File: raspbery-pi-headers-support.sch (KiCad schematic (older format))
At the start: 15 parts, among them J1 RasPi-CM3-Headers, J10 500901-0801, J11 HDMI-A-connector, U38 DMG1012T, U39 DMG1012T, U40 ESD7484, U41 ESD7484, U42 ESD5384, U43 AP2331X

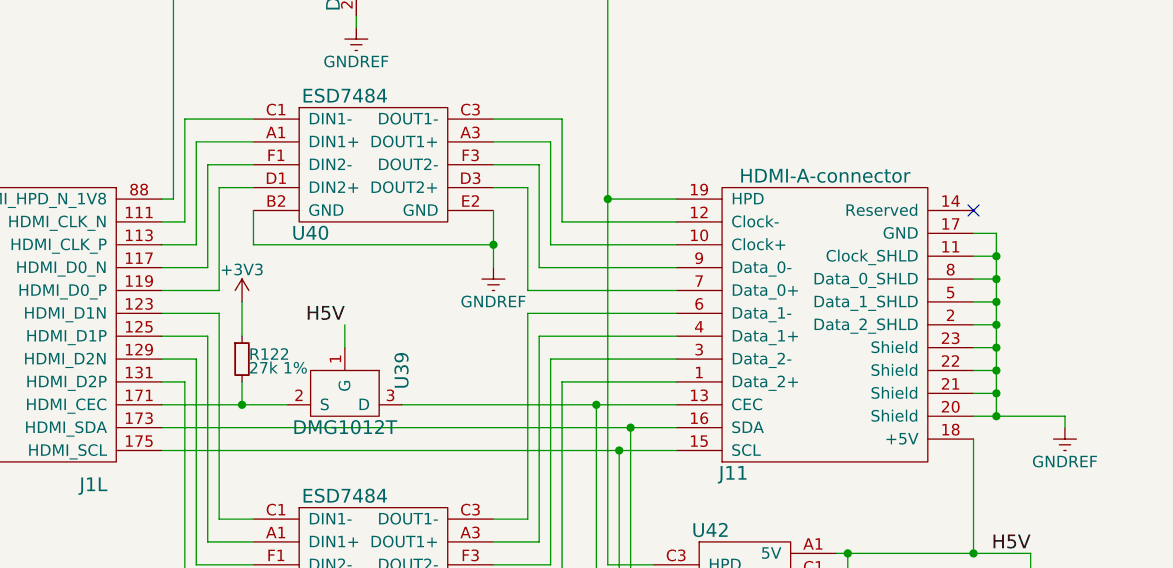
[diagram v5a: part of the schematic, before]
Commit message: Fixing issues with pin numbering between footprint and symbol
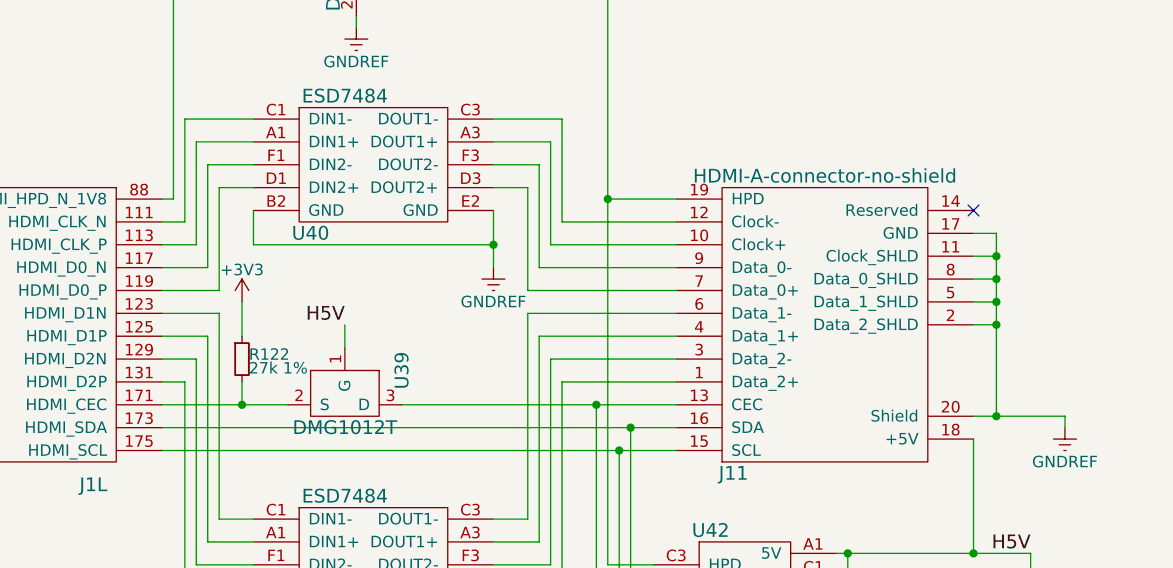
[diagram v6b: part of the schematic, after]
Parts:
- removed J11: HDMI-A-connector, Pin_Headers:Pin_Header_Straight_2x10_Pitch1.27mm, symbol HDMI-A-connector
- added J11: HDMI-A-connector-no-shield, Pin_Headers:Pin_Header_Straight_2x10_Pitch1.27mm, symbol HDMI-A-connector-no-shield
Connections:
- net GNDREF: now also J11.11 (Clock_SHLD), J11.17 (GND), J11.2 (Data_2_SHLD), J11.20 (Shield), J11.5 (Data_1_SHLD), J11.8 (Data_0_SHLD)
- net H5V: now also J11.18 (+5V)
- net at J1.173 (HDMI_SDA), U42.B3 (SDA): now also J11.16 (SDA)
- net at J1.175 (HDMI_SCL), U42.A3 (SCL): now also J11.15 (SCL)
- net at U41.D3 (DOUT2+): now also J11.1 (Data_2+)
- net at U40.A3 (DOUT1+): now also J11.10 (Clock+)
- net at U40.C3 (DOUT1-): now also J11.12 (Clock-)
- net at U39.3 (D), U42.A2 (CEC): now also J11.13 (CEC)
- net at U38.1 (G), U42.C3 (HPD): now also J11.19 (HPD)
- net at U41.F3 (DOUT2-): now also J11.3 (Data_2-)
- net at U41.A3 (DOUT1+): now also J11.4 (Data_1+)
- net at U41.C3 (DOUT1-): now also J11.6 (Data_1-)
- net at U40.D3 (DOUT2+): now also J11.7 (Data_0+)
- net at U40.F3 (DOUT2-): now also J11.9 (Data_0-)
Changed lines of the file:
@@
-$EndComp
-$Comp
-L HDMI-A-connector J11
-U 1 1 5911658C
-P 5450 2950
-F 0 "J11" H 5050 3600 60  0000 C CNN
-F 1 "HDMI-A-connector" H 5450 2300 60  0000 C CNN
-F 2 "Pin_Headers:Pin_Header_Straight_2x10_Pitch1.27mm" H 5450 2950 60  0001 C CNN
-F 3 "" H 5450 2950 60  0001 C CNN
-F 4 "0.00@0" H 5500 3850 60  0001 C CNN "Pricing"
-F 5 "Generic HDMI Connector pinout" H 5500 3750 60  0001 C CNN "Description"
-	1    5450 2950
-	1    0    0    1
 $EndComp
 $Comp
@@
 Wire Wire Line
 	6100 3350 6500 3350
-Wire Wire Line
-	6100 3250 6200 3250
-Connection ~ 6200 3250
-Wire Wire Line
-	6100 3150 6200 3150
-Connection ~ 6200 3150
-Wire Wire Line
-	6100 3050 6200 3050
-Connection ~ 6200 3050
 Wire Wire Line
 	6100 2950 6200 2950
@@
 $EndComp
 Wire Wire Line
-	3100 3300 2550 3300
+	2550 3300 3100 3300
 Text Label 3350 2950 2    60   ~ 0
 H5V
@@
 	2900 2850 2900 3000
 NoConn ~ 6100 2450
+$Comp
+L HDMI-A-connector-no-shield J11
+U 1 1 59200D14
+P 5450 2950
+F 0 "J11" H 5050 3600 60  0000 C CNN
+F 1 "HDMI-A-connector-no-shield" H 5450 2300 60  0000 C CNN
+F 2 "Pin_Headers:Pin_Header_Straight_2x10_Pitch1.27mm" H 5450 2950 60  0001 C CNN
+F 3 "" H 5450 2950 60  0001 C CNN
+F 4 "Generic HDMI Connector pinout" H 5500 3750 60  0001 C CNN "Description"
+F 5 "0.00@0" H 5500 3850 60  0001 C CNN "Pricing"
+	1    5450 2950
+	1    0    0    1
+$EndComp
 $EndSCHEMATC

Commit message: More work on pcb layout
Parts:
- R122, R123: footprint Resistors_SMD:R_0603 -> Resistors_SMD:R_0402_NoSilk
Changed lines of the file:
@@
 F 0 "R123" H 3430 920 50  0000 L CNN
 F 1 "100k 1%" H 3430 860 50  0000 L CNN
-F 2 "Resistors_SMD:R_0603" H 3400 900 50  0001 C CNN
+F 2 "Resistors_SMD:R_0402_NoSilk" H 3400 900 50  0001 C CNN
 F 3 "" H 3400 900 50  0001 C CNN
 	1    3400 900
@@
 F 0 "R122" H 2930 3120 50  0000 L CNN
 F 1 "27k 1%" H 2930 3060 50  0000 L CNN
-F 2 "Resistors_SMD:R_0603" H 2900 3100 50  0001 C CNN
+F 2 "Resistors_SMD:R_0402_NoSilk" H 2900 3100 50  0001 C CNN
 F 3 "" H 2900 3100 50  0001 C CNN
 	1    2900 3100
